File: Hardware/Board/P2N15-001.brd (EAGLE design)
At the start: 72 x 72 mm, 36 parts, among them IC1 4053N, IC2 LTC485N, IC3 74LS07N, IC4 LTC485N, X1 HIROSE-DX10LM1-14SE, X2 SUNHAYATO-USB-CK37

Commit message: Redesigned N15 board.
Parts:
- removed IC3: 74LS07N, 74xx-us:DIL14
- removed IC4: LTC485N, linear-technology:DIL08
- removed JP3: (no value), pinhead:2X03
- removed JP4: (no value), adafruit:1X06
- removed LED1, LED2: (no value), led:LED3MM
- removed R10, R11, R12, R7, R8, R9: 220, resistor:0204/5
- removed R13, R6: 120, resistor:0204/5
- added S2: TL32PO, switch:TL3XPO
- added SV2: (no value), con-ml:ML10L
- IC1: value 4053N -> TLC5941NT; device 40xx:DIL16 -> adafruit:DIL28-3
- R3: value 330 -> 4.7k
- R4: value 330 -> 120
- SV1: device con-ml:ML10L -> con-ml:ML20L
- moved IC2 43.8 mm to (12.7, 53.3)
- moved OK1 43.2 mm to (35.6, 53.3)
- moved D1 34.2 mm to (43.2, 53.3)
- moved C2 33.5 mm to (7.62, 36.8)
- moved R4 29.6 mm to (43.2, 36.8), turned to 90 degrees
- moved C3 27.1 mm to (38.1, 36.8)
- moved C5 23.4 mm to (27.9, 36.8)
- moved SV1 19.7 mm to (22.9, 11.4), turned to 180 degrees
- moved R5 17.3 mm to (20.3, 38.1)
- moved R3 16.9 mm to (40.6, 12.7)
- moved C4 16.5 mm to (3.81, 49.5)
- moved IC1 8.89 mm to (26.7, 21.6)
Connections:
- removed net ANLG0: JP2.8, MC1.P$31, X1.P$8
- removed net ANLG1: JP2.9, MC1.P$30, X1.P$9
- removed net ANLG2: JP2.10, MC1.P$29, X1.P$10
- removed net ANLG3: JP2.11, MC1.P$28, X1.P$11
- removed net ANLG4: IC1.13, MC1.P$27
- removed net ANLG5: IC1.1, MC1.P$26
- removed net MISO: JP3.4, MC1.P$19
- removed net RXRETURN: R5.2, SV1.3
- removed net RXSEND: R10.2, SV1.1
- removed net SCL: IC1.2, MC1.P$10
- removed net SDA: IC1.12, MC1.P$11
- removed net SEL: IC1.10, IC1.11, MC1.P$6
- removed net TX: IC3.1, IC3.3, IC4.4, MC1.P$15
- removed net TX+: CN1.1, IC4.6, R13.2
- removed net TX-: CN1.2, IC4.7, R13.1
- removed net TX2RETURN: R11.2, SV1.5
- removed net TX2SEND: R9.2, SV1.4
- removed net TXRETURN: R12.2, SV1.8
- removed net TXSEND: R8.2, SV1.6
- removed net VEE: IC1.7
- removed net XMIDIRX: IC1.3, IC2.1
- new net N$10: IC1.3, JP2.10, SV1.6, X1.P$10
- new net N$11: IC1.4, JP2.11, SV1.7, X1.P$11
- new net N$12: IC1.10, SV1.14
- new net N$13: IC1.11, SV1.13
- new net N$14: IC1.12, SV1.16
- new net N$16: IC1.13, SV1.15
- new net N$7: IC1.1, JP2.8, SV1.4, X1.P$8
- new net N$9: IC1.2, JP2.9, SV1.5, X1.P$9
- net GND: now also IC1.22, IC1.27, R3.1, SV1.1; no longer IC1.6, IC1.8, IC3.11, IC3.13, IC3.7, IC3.9, IC4.5, JP2.14, JP4.5, R3.2, R4.2, SV1.2, SV1.7, X1.P$14
- net GPIO0: now also IC1.18; no longer JP3.1, LED1.A
- net GPIO1: now also IC1.23; no longer JP3.2, LED2.A
- net GPIO2: now also IC1.24; no longer JP3.3
- net MIDIRX: now also S2.1; no longer IC1.5, IC3.5
- net MOSI: now also IC1.26; no longer JP3.5
- net N$15: now also R5.1; no longer R7.1
- net N$17: now also IC1.14, SV1.18; no longer LED1.K, R3.1
- net N$18: now also IC1.15, SV1.17; no longer LED2.K, R4.1
- net N$2: now also IC2.1, S2.3; no longer IC3.2, R11.1
- net N$28: now also IC1.5, SV1.8; no longer IC1.14
- net N$29: now also IC1.6, SV1.9; no longer IC1.15
- net N$3: now also IC1.28, JP2.7, SV1.3, X1.P$7; no longer IC3.6, R5.1
- net N$4: now also IC1.20, R3.2; no longer IC3.4, R12.1
- net N$5: now also IC1.7, JP2.14, SV1.10, X1.P$14; no longer JP4.2, MC1.P$4
- net N$6: now also IC1.8, SV1.12; no longer JP4.3, MC1.P$3
- net N$8: now also SV1.11; no longer MC1.P$9
- net PD: no longer JP4.1
- net RX: now also S2.2
- net RX+: now also R4.2; no longer R6.2
- net RX-: now also R4.1; no longer R6.1
- net RXA: now also R5.2, SV2.9; no longer R7.2, SV1.9
- net RXK: now also SV2.10; no longer SV1.10
- net SCLK: now also IC1.25; no longer JP3.6
- net VCC: now also IC1.19, IC1.21; no longer IC1.16, IC3.14, IC4.2, IC4.3, IC4.8, JP2.7, R10.1, R8.1, R9.1, X1.P$7
- net VDD: now also SV1.2
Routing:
- net TXRETURN: track 175.1 -> 0.00 mm, vias 4 -> 0
- net RXA: track 13.5 -> 174.8 mm, vias 0 -> 6
- net ANLG3: track 148.7 -> 0.00 mm, vias 3 -> 0
- net N$11: track 0.00 -> 135.9 mm, vias 0 -> 2
- net TX2RETURN: track 129.4 -> 0.00 mm, vias 5 -> 0
- net N$9: track 0.00 -> 124.9 mm, vias 0 -> 6
- net SCL: track 118.5 -> 0.00 mm, vias 7 -> 0
- net RXRETURN: track 118.4 -> 0.00 mm, vias 5 -> 0
- net N$7: track 0.00 -> 116.8 mm, vias 0 -> 5
- net VCC: track 240.2 -> 129.8 mm, vias 2 -> 0
- net GPIO2: track 169.2 -> 64.9 mm, vias 4 -> 2
- net RXK: track 45.9 -> 145.8 mm, vias 0 -> 2
- net GND: track 359.6 -> 259.9 mm, vias 3 -> 2
- net N$10: track 0.00 -> 93.2 mm, vias 0 -> 3
- net MIDIRX: track 104.0 -> 18.4 mm, vias 1 -> 0
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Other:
- board text added: "PINEAPPLE II NITROGEN 15 REVISION 1.0.0 (2015)"
- board text removed: "PINEAPPLE II NITROGEN 14 REVISION 1.0.0 (2015)"

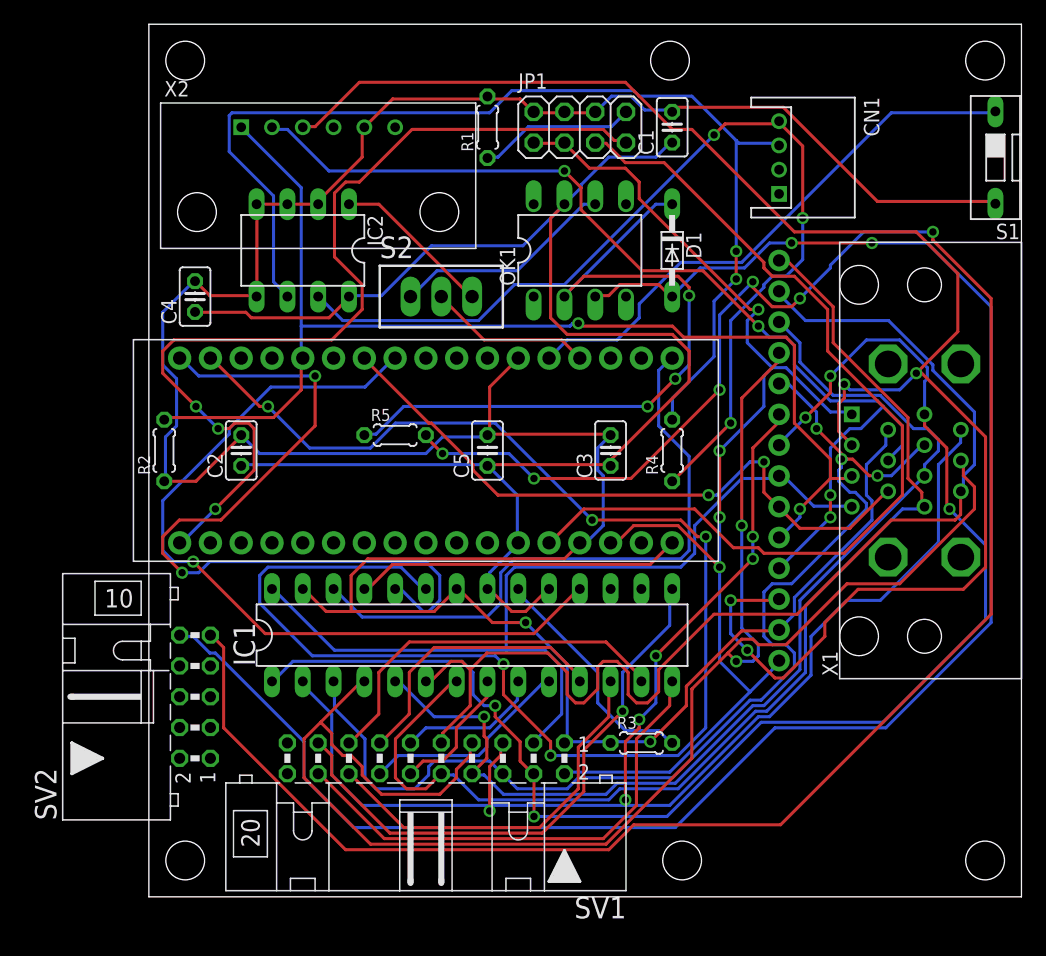
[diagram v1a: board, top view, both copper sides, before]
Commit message: Changed 20-p MIL connector type from right-angled to straight.
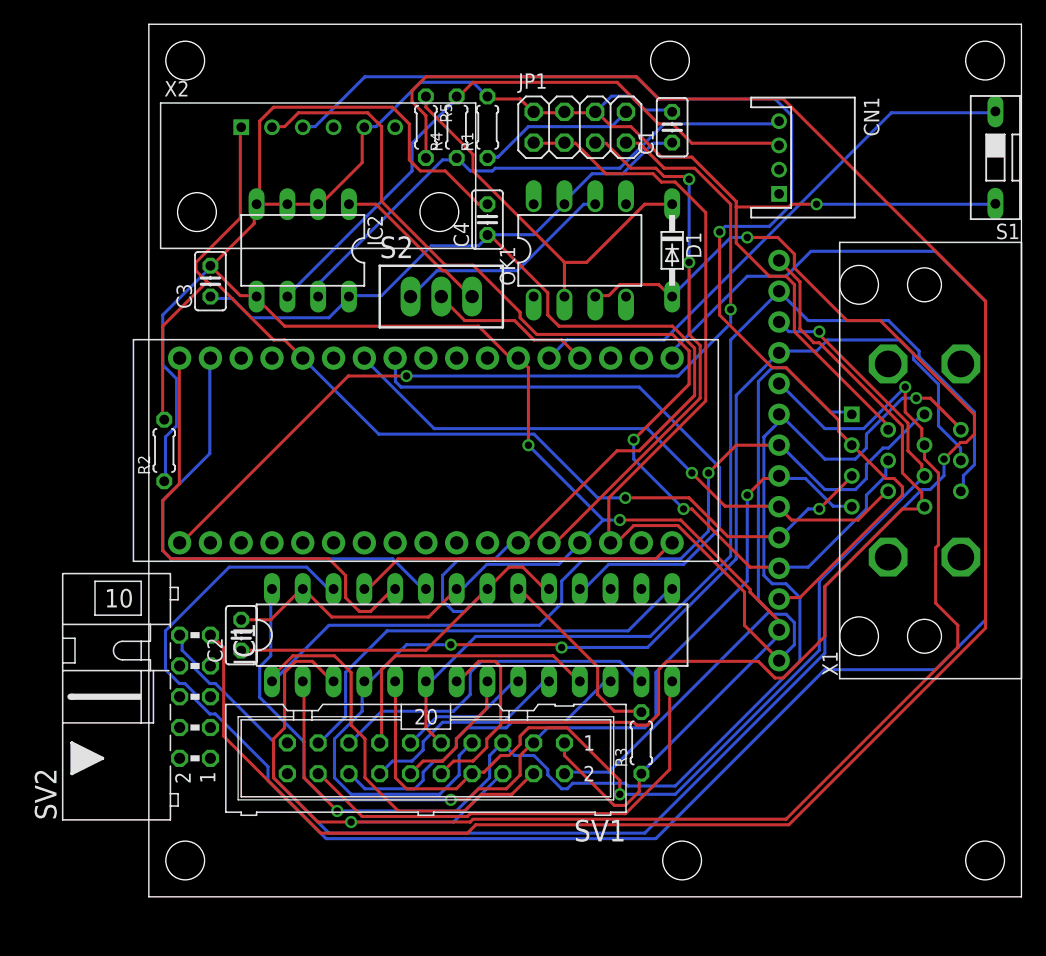
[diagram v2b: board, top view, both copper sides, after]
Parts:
- removed C5: 103, rcl:C025-025X050
- SV1: device con-ml:ML20L -> con-ml:ML20
- moved C3 35.9 mm to (5.08, 50.8)
- moved R4 32.1 mm to (25.4, 63.5)
- moved R5 25.5 mm to (22.9, 63.5), turned to 270 degrees
- moved C4 25.0 mm to (27.9, 55.9)
- moved C2 15.2 mm to (7.62, 21.6)
- turned R3 to 90 degrees
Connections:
- net GND: no longer C5.2
- net VCC: no longer C5.1
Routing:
- net MOSI: track 51.5 -> 159.7 mm
- net GPIO1: track 126.7 -> 40.6 mm, vias 5 -> 0
- net RX+: track 90.3 -> 51.5 mm, vias 2 -> 0
- net N$11: track 135.9 -> 99.5 mm
- net USBD+: track 136.4 -> 100.4 mm, vias 4 -> 1
- net N$10: track 93.2 -> 129.1 mm, vias 3 -> 2
- net RX-: track 81.3 -> 45.7 mm, vias 3 -> 0
- net RST: track 76.8 -> 44.8 mm, vias 0 -> 2
- net GND: track 259.9 -> 288.2 mm, vias 2 -> 3
- net N$15: track 59.1 -> 32.1 mm, vias 3 -> 0
- net GPIO2: track 64.9 -> 39.5 mm, vias 2 -> 0
- net VDD: track 101.8 -> 125.8 mm, vias 4 -> 0
- net N$9: track 124.9 -> 103.3 mm, vias 6 -> 2
- net GPIO0: track 67.2 -> 50.3 mm, vias 1 -> 0
- net N$7: track 116.8 -> 104.2 mm, vias 5 -> 1
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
